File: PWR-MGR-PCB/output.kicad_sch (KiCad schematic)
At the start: 7 parts, among them J1 Conn_01x02_Pin, J2 Conn_01x02_Pin, J5 Conn_01x02_Pin

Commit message: begin v2, update schematic
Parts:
- removed J1: Conn_01x02_Pin, Connector_JST:JST_XH_B2B-XH-A_1x02_P2.50mm_Vertical, symbol Connector:Conn_01x02_Pin
- removed J5: Conn_01x02_Pin, Connector_PinHeader_2.00mm:PinHeader_1x02_P2.00mm_Vertical, symbol Connector:Conn_01x02_Pin
- added J10, J11, J12, J13, J14, J4, J6, J7, J8, J9: Conn_01x01_Socket, Custom_Footprints:Drilled_Solder_Pad_0.6mm_3x1mm, symbol Connector:Conn_01x01_Socket
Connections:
- net 3.3V: now also J4.1 (Pin_1), J9.1 (Pin_1)
- net GND: now also J10.1 (Pin_1), J12.1 (Pin_1), J14.1 (Pin_1), J6.1 (Pin_1)
- net USB_D+: now also J7.1 (Pin_1)
- net USB_D-: now also J8.1 (Pin_1)
- new net 5V: J11.1 (Pin_1), J13.1 (Pin_1)
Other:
- note added: "I/O Pads"
- note removed: "3.3V Power Port"
- moved on the sheet: H5, H6, H7, H8, J2

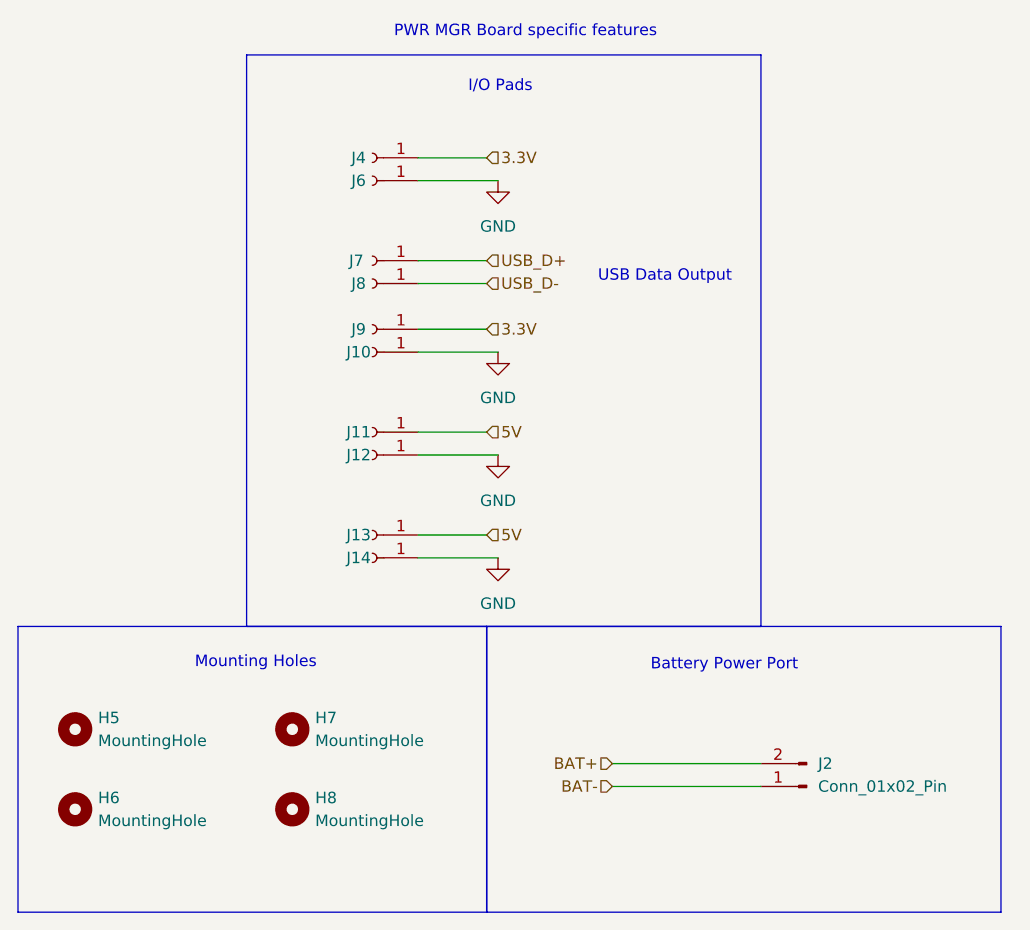
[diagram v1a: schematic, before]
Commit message: complete schematic
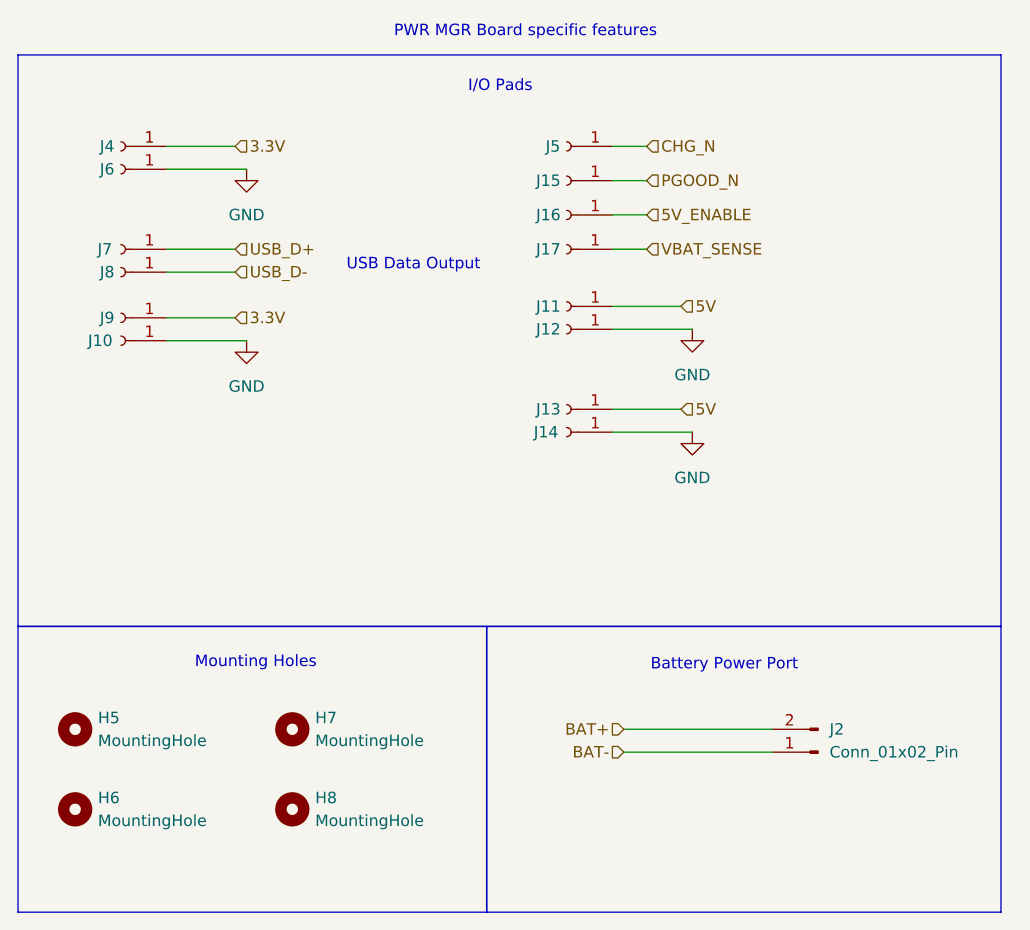
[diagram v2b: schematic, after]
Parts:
- added J15, J16, J17, J5: Conn_01x01_Socket, Custom_Footprints:Drilled_Solder_Pad_0.6mm_3x1mm, symbol Connector:Conn_01x01_Socket
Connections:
- new net 5V_ENABLE: J16.1 (Pin_1)
- new net CHG_N: J5.1 (Pin_1)
- new net PGOOD_N: J15.1 (Pin_1)
- new net VBAT_SENSE: J17.1 (Pin_1)
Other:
- moved on the sheet: J10, J11, J12, J13, J14, J2, J4, J6, J7, J8, J9

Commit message: route regulators
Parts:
- removed J2: Conn_01x02_Pin, Connector_JST:JST_XH_B2B-XH-A_1x02_P2.50mm_Vertical, symbol Connector:Conn_01x02_Pin
- added J18, J19, J20, J21, J22, J23, J24, J25, J26, J27: Conn_01x01_Socket, Custom_Footprints:Drilled_Solder_Pad_0.6mm_3x1mm, symbol Connector:Conn_01x01_Socket
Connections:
- net 3.3V: now also J20.1 (Pin_1), J22.1 (Pin_1)
- net 5V: now also J18.1 (Pin_1)
- net BAT+: now also J26.1 (Pin_1)
- net BAT-: now also J27.1 (Pin_1)
- net GND: now also J19.1 (Pin_1), J21.1 (Pin_1), J23.1 (Pin_1), J24.1 (Pin_1), J25.1 (Pin_1)

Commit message: route signals
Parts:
- removed J25, J4: Conn_01x01_Socket, Custom_Footprints:Drilled_Solder_Pad_0.6mm_3x1mm, symbol Connector:Conn_01x01_Socket
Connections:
- net 5V_ENABLE: now also J17.1 (Pin_1); no longer J16.1 (Pin_1)
- net VBAT_SENSE: now also J16.1 (Pin_1); no longer J17.1 (Pin_1)
